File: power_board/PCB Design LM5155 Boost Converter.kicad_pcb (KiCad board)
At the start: 2 copper layers, 80 x 53 mm, 71 parts, among them Q1 BSC035N04LS G, U1 LM5155_DSSR

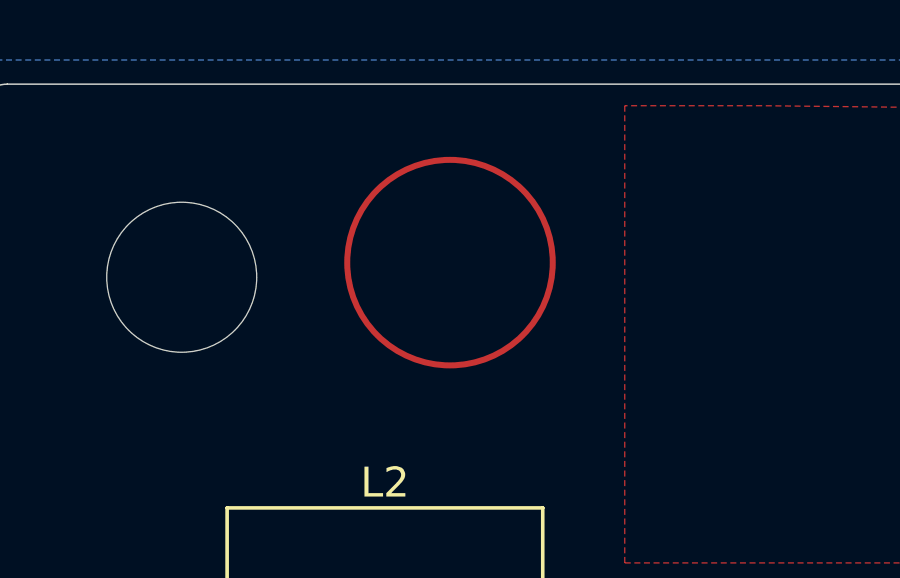
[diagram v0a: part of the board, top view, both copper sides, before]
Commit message: 2 Layer to 4 Layer PCB
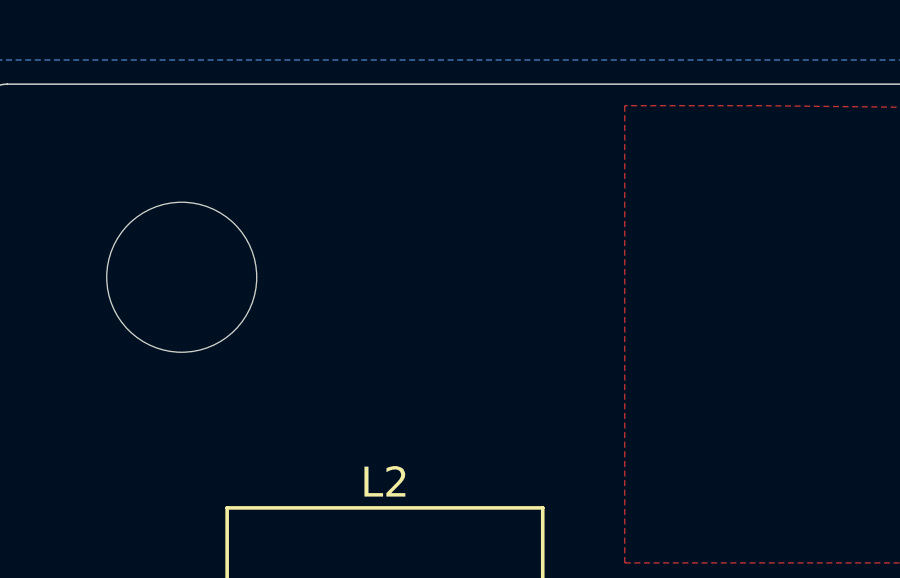
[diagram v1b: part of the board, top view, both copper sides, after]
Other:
- copper layers 2 -> 4
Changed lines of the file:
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@@
 	(layers
 		(0 "F.Cu" signal)
+		(4 "In1.Cu" signal)
+		(6 "In2.Cu" signal)
 		(2 "B.Cu" signal)
 		(9 "F.Adhes" user "F.Adhesive")
@@
 			)
 			(layer "dielectric 1"
+				(type "prepreg")
+				(thickness 0.1)
+				(material "FR4")
+				(epsilon_r 4.5)
+				(loss_tangent 0.02)
+			)
+			(layer "In1.Cu"
+				(type "copper")
+				(thickness 0.035)
+			)
+			(layer "dielectric 2"
 				(type "core")
-				(thickness 1.51)
+				(thickness 1.24)
+				(material "FR4")
+				(epsilon_r 4.5)
+				(loss_tangent 0.02)
+			)
+			(layer "In2.Cu"
+				(type "copper")
+				(thickness 0.035)
+			)
+			(layer "dielectric 3"
+				(type "prepreg")
+				(thickness 0.1)
 				(material "FR4")
 				(epsilon_r 4.5)
@@
 		(capping no)
 		(filling no)
+		(zone_defaults)
 		(pcbplotparams
 			(layerselection 0x00000000_00000000_55555555_5755f5ff)
@@
 		)
 	)
-	(gr_circle
-		(center 118 57.3)
-		(end 119.9 60.15)
-		(stroke
-			(width 0.2)
-			(type default)
-		)
-		(fill no)
-		(layer "F.Cu")
-	)
 	(gr_arc
